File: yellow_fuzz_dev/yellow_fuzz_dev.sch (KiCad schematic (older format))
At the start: 39 parts

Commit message: pulling parts in for schematic capture
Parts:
- added C?: 47n, Capacitor_SMD:C_0603_1608Metric_Pad1.05x0.95mm_HandSolder, symbol Device:C
- added CON?: SN49B12B, digikey-footprints:Headphone_Jack_6.35mm_SN49B12B, symbol dk_Barrel-Audio-Connectors:SN49B12B
- added D?: WP7113QBC_D, digikey-footprints:LED_5mm_Radial, symbol dk_LEDs:WP7113QBC_D
- added J?: RA49B11, yellow_fuzz_dev:Headphone_Jack_6.35mm_SN49B12B, symbol yellow_fuzz_dev:RA49B11
- added Q?: NSVJ3910SB3T1GOSCT-ND, Package_TO_SOT_SMD:SOT-23_Handsoldering, symbol yellow_fuzz_dev:NSVJ3910SB3T1GOSCT-ND
- added Q?: BC817-25-TP, digikey-footprints:SOT-23-3, symbol dk_NPN_Single:BC817-25-TP
- added R? (x2): 10k, Resistor_SMD:R_0603_1608Metric_Pad1.05x0.95mm_HandSolder, symbol Device:R
- added R?: 1M, Resistor_SMD:R_0603_1608Metric_Pad1.05x0.95mm_HandSolder, symbol Device:R
- added U? (x5): TL074, digikey:SOIC-14_W3.9mm, symbol Amplifier_Operational:TL074
- RV?: footprint Potentiometer_THT:Potentiometer_Alps_RK09L_Single_Vertical -> yellow_fuzz_dev:Potentiometer_Bourns_PCW1J_R24_B_Single_Vertical; Manufacturer ALPS -> Bourns; Manufacturer PN RK09L1140A5P -> PTV111-4420A-A503; Supplier PN 688-RK09L1140A5P -> 652-PTV111-4420AA503; Taper Linear -> Log
- RV?: footprint Potentiometer_THT:Potentiometer_Alps_RK09Y11_Single_Horizontal -> yellow_fuzz_dev:Potentiometer_Bourns_PCW1J_R24_B_Single_Vertical; Manufacturer ALPS -> Bourns; Manufacturer PN RK09L1140A65 -> PCW1J-R24-BAD252; Supplier PN 688-RK09L1140A65 -> 652-PCW1J-R24-BAD252; Taper Linear -> Log; Value 5k -> 2.5k
- RV?: footprint Potentiometer_THT:Potentiometer_Alps_RK09L_Double_Vertical -> yellow_fuzz_dev:Potentiometer_Bourns_PTV112_3417A_Dual_Vertical; Manufacturer ALPS -> Bourns; Manufacturer PN RK09L124000Z -> PTV112-4420A-A503; Supplier PN 688-RK09L124000Z -> 652-PTV112-4420AA503; Taper Linear -> Log
- RV?: footprint Potentiometer_THT:Potentiometer_Alps_RK09L_Double_Vertical -> yellow_fuzz_dev:Potentiometer_Bourns_PTV112_3417A_Dual_Vertical; Manufactuerer PN RK09L124000Z -> PTV112-4420A-A503; Manufacturer ALPS -> Bourns; Supplier PN 688-RK09L124000Z -> 652-PTV112-4420AA503; Taper Linear -> Log
- RV?: footprint Potentiometer_THT:Potentiometer_Alps_RK09L_Single_Vertical -> Potentiometer_THT:Potentiometer_Bourns_PTV09A-1_Single_Vertical; Manufacturer ALPS -> Bourns; Manufacturer PN RK09D113BF25B15 -> PTV09A-4030U-A204; Supplier PN 688-RK09D113BF25B15 -> 652-PTV09A-4030UA204; Taper Linear -> Log; Value 100k -> 200k
- RV?: footprint Potentiometer_THT:Potentiometer_TT_P0915N -> yellow_fuzz_dev:Potentiometer_Bourns_PTV111_4420A_Single_Vertical; Manufacturer (none) -> Bourns; Manufacturer PN (none) -> PTV111-4420A-A104; Supplier (none) -> Mouser; Supplier PN (none) -> 652-PTV111-4420AA104; Value 250k -> 100k
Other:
- moved on the sheet: C?, R?, RV?, RV?A, RV?B

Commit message: schematic capture in progress
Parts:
- removed U?: TL074, digikey:SOIC-14_W3.9mm, symbol Amplifier_Operational:TL074
- added C? (x3): 1u, symbol Device:CP1
- added C? (x3): 15n, Capacitor_SMD:C_0603_1608Metric_Pad1.05x0.95mm_HandSolder, symbol Device:C
- added C? (x2): 47n, Capacitor_SMD:C_0603_1608Metric_Pad1.05x0.95mm_HandSolder, symbol Device:C
- added C?: 33n, Capacitor_SMD:C_0603_1608Metric_Pad1.05x0.95mm_HandSolder, symbol Device:C
- added C?: 220p, Capacitor_SMD:C_0603_1608Metric_Pad1.05x0.95mm_HandSolder, symbol Device:C
- added C?: 27n, Capacitor_SMD:C_0603_1608Metric_Pad1.05x0.95mm_HandSolder, symbol Device:C
- added C?: 10n, Capacitor_SMD:C_0603_1608Metric_Pad1.05x0.95mm_HandSolder, symbol Device:C
- added C? (x2): 47p, Capacitor_SMD:C_0603_1608Metric_Pad1.05x0.95mm_HandSolder, symbol Device:C
- added C? (x4): 10u, symbol Device:CP1
- added C?: 10p, Capacitor_SMD:C_0603_1608Metric_Pad1.05x0.95mm_HandSolder, symbol Device:C
- added C?: 220n, symbol Device:CP1
- added C?: 1.5n, Capacitor_SMD:C_0603_1608Metric_Pad1.05x0.95mm_HandSolder, symbol Device:C
- added D? (x2): 1N4148, digikey-footprints:Diode_DO-35_P10mm, symbol dk_Diodes-Rectifiers-Single:1N4148
- added Q? (x2): NSVJ3910SB3T1GOSCT-ND, Package_TO_SOT_SMD:SOT-23_Handsoldering, symbol yellow_fuzz_dev:NSVJ3910SB3T1GOSCT-ND
- added Q? (x4): BC817-25-TP, digikey-footprints:SOT-23-3, symbol dk_NPN_Single:BC817-25-TP
- added R? (x6): 100k, Resistor_SMD:R_0603_1608Metric_Pad1.05x0.95mm_HandSolder, symbol Device:R
- added R? (x2): 1M, Resistor_SMD:R_0603_1608Metric_Pad1.05x0.95mm_HandSolder, symbol Device:R
- added R? (x9): 10k, Resistor_SMD:R_0603_1608Metric_Pad1.05x0.95mm_HandSolder, symbol Device:R
- added R?: 220k, Resistor_SMD:R_0603_1608Metric_Pad1.05x0.95mm_HandSolder, symbol Device:R
- added R? (x2): 47k, Resistor_SMD:R_0603_1608Metric_Pad1.05x0.95mm_HandSolder, symbol Device:R
- added R? (x2): 2.2k, Resistor_SMD:R_0603_1608Metric_Pad1.05x0.95mm_HandSolder, symbol Device:R
- added R? (x3): 1k, Resistor_SMD:R_0603_1608Metric_Pad1.05x0.95mm_HandSolder, symbol Device:R
- added R?: 4.7k, Resistor_SMD:R_0603_1608Metric_Pad1.05x0.95mm_HandSolder, symbol Device:R
- added R? (x3): 22k, Resistor_SMD:R_0603_1608Metric_Pad1.05x0.95mm_HandSolder, symbol Device:R
- added R?: 3.3k, Resistor_SMD:R_0603_1608Metric_Pad1.05x0.95mm_HandSolder, symbol Device:R
- added R?: 470k, Resistor_SMD:R_0603_1608Metric_Pad1.05x0.95mm_HandSolder, symbol Device:R
- added U?: TL074, symbol Amplifier_Operational:TL074
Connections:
- net labels added: +4V5, +9V, GND
- wire segments 0 -> 186
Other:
- note added: "Here Lies Clippy"
- note added: "Input Buffer"
- note added: "Post Distortion"
- note added: "Pre-Distortion"
- moved on the sheet: C?, J?, Q?, R?, RV?, RV?A, RV?B, U?B, U?C, U?D, U?E

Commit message: placing symbols for EQ section
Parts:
- removed RV?: R_POT_Dual_Separate, yellow_fuzz_dev:Potentiometer_Bourns_PTV112_3417A_Dual_Vertical, symbol Device:R_POT_Dual_Separate
- added C?: 10p, Capacitor_SMD:C_0603_1608Metric_Pad1.05x0.95mm_HandSolder, symbol Device:C
- added C? (x2): 1u, symbol Device:CP1
- added C?: 100p, Capacitor_SMD:C_0603_1608Metric_Pad1.05x0.95mm_HandSolder, symbol Device:C
- added C?: 10n, Capacitor_SMD:C_0603_1608Metric_Pad1.05x0.95mm_HandSolder, symbol Device:C
- added C?: 220n, symbol Device:CP1
- added C?: 47n, Capacitor_SMD:C_0603_1608Metric_Pad1.05x0.95mm_HandSolder, symbol Device:C
- added C?: 0.1u, Capacitor_SMD:C_0603_1608Metric_Pad1.05x0.95mm_HandSolder, symbol Device:C
- added C?: 8.2n, Capacitor_SMD:C_0603_1608Metric_Pad1.05x0.95mm_HandSolder, symbol Device:C
- added C?: 22n, Capacitor_SMD:C_0603_1608Metric_Pad1.05x0.95mm_HandSolder, symbol Device:C
- added C?: 10u, symbol Device:CP1
- added R?: 22k, Resistor_SMD:R_0603_1608Metric_Pad1.05x0.95mm_HandSolder, symbol Device:R
- added R? (x2): 47k, Resistor_SMD:R_0603_1608Metric_Pad1.05x0.95mm_HandSolder, symbol Device:R
- added R? (x2): 330, Resistor_SMD:R_0603_1608Metric_Pad1.05x0.95mm_HandSolder, symbol Device:R
- added R? (x3): 2.2k, Resistor_SMD:R_0603_1608Metric_Pad1.05x0.95mm_HandSolder, symbol Device:R
- added R?: 100k, Resistor_SMD:R_0603_1608Metric_Pad1.05x0.95mm_HandSolder, symbol Device:R
- added R?: 1M, Resistor_SMD:R_0603_1608Metric_Pad1.05x0.95mm_HandSolder, symbol Device:R
- added RV? (x3): R_POT_US, yellow_fuzz_dev:Potentiometer_Bourns_PTV111_4420A_Single_Vertical, symbol Device:R_POT_US
- added RV?: R_POT_Dual_Separate, yellow_fuzz_dev:Potentiometer_Bourns_PTV112_3417A_Dual_Vertical, symbol Device:R_POT_Dual_Separate
- added U?: TL074, symbol Amplifier_Operational:TL074
- added U? (x4): TL074, digikey:SOIC-14_W3.9mm, symbol Amplifier_Operational:TL074
- CON?: symbol dk_Barrel-Audio-Connectors:SN49B12B -> yellow_fuzz_dev-rescue:SN49B12B-dk_Barrel-Audio-Connectors
- D? (x2): symbol dk_Diodes-Rectifiers-Single:1N4148 -> yellow_fuzz_dev-rescue:1N4148-dk_Diodes-Rectifiers-Single
- D?: symbol dk_LEDs:WP7113QBC_D -> yellow_fuzz_dev-rescue:WP7113QBC_D-dk_LEDs
- Q? (x5): symbol dk_NPN_Single:BC817-25-TP -> yellow_fuzz_dev-rescue:BC817-25-TP-dk_NPN_Single
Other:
- note removed: "Here Lies Clippy"
- note removed: "Input Buffer"
- note removed: "Post Distortion"
- note removed: "Pre-Distortion"
- moved on the sheet: RV?, RV?B

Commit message: captured tone, power, and switching sections.
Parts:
- added C?: 1u, symbol Device:CP1
- added C? (x3): 100u, symbol Device:CP1
- added C?: 47n, Capacitor_SMD:C_0603_1608Metric_Pad1.05x0.95mm_HandSolder, symbol Device:C
- added C?: 10n, Capacitor_SMD:C_0603_1608Metric_Pad1.05x0.95mm_HandSolder, symbol Device:C
- added C? (x2): 220p, Capacitor_SMD:C_0603_1608Metric_Pad1.05x0.95mm_HandSolder, symbol Device:C
- added C? (x2): 470p, Capacitor_SMD:C_0603_1608Metric_Pad1.05x0.95mm_HandSolder, symbol Device:C
- added D? (x3): BAS16W, Package_TO_SOT_SMD:SOT-323_SC-70, symbol Diode:BAS16W
- added D?: DZ2S056X0L, Diode_SMD:D_SOD-523, symbol Diode:DZ2S056X0L
- added J?: Barrel_Jack_Switch, symbol Connector:Barrel_Jack_Switch
- added Q?: NSVJ3910SB3T1GOSCT-ND, Package_TO_SOT_SMD:SOT-23_Handsoldering, symbol yellow_fuzz_dev:NSVJ3910SB3T1GOSCT-ND
- added Q? (x2): BC817-25-TP, digikey-footprints:SOT-23-3, symbol yellow_fuzz_dev-rescue:BC817-25-TP-dk_NPN_Single
- added Q? (x2): DMG2301L, Package_TO_SOT_SMD:SOT-23, symbol Transistor_FET:DMG2301L
- added R?: 2.2k, Resistor_SMD:R_0603_1608Metric_Pad1.05x0.95mm_HandSolder, symbol Device:R
- added R? (x4): 1M, Resistor_SMD:R_0603_1608Metric_Pad1.05x0.95mm_HandSolder, symbol Device:R
- added R?: 1.2k, Resistor_SMD:R_0603_1608Metric_Pad1.05x0.95mm_HandSolder, symbol Device:R
- added R? (x2): 10k, Resistor_SMD:R_0603_1608Metric_Pad1.05x0.95mm_HandSolder, symbol Device:R
- added R?: 100, Resistor_SMD:R_0603_1608Metric_Pad1.05x0.95mm_HandSolder, symbol Device:R
- added R? (x2): 100k, Resistor_SMD:R_0603_1608Metric_Pad1.05x0.95mm_HandSolder, symbol Device:R
- added R? (x4): 56k, Resistor_SMD:R_0603_1608Metric_Pad1.05x0.95mm_HandSolder, symbol Device:R
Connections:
- net +4V: now also R?.2, R?.2, C?.1, C?.1, R?.1, R?.1, R?.1, R?.2
- net +9V: now also C?.1, D?.1 (K), R?.1, R?.1, R?.1, R?.1
- net GND: now also C?.2, C?.2, R?.2, RV?.1, C?.2, C?.2, C?.2, C?.2, C?.2, Q?.2 (E), Q?.2 (E), R?.2, R?.2, R?.2
- net at RV?.2: now also C?.2
- net at RV?.3: now also C?.2
- net at RV?.4: now also C?.1, C?.1, RV?.1, RV?.2, RV?.5
- net at RV?.6: now also R?.1
- net at Q?.3 (G): now also D?.1 (A) (x2)
- net at D?.1: now also R?.2
- net at U?.1: now also R?.2, U?.2 (-)
- net at U?.3 (+): now also C?.2, R?.1
- net at U?.5 (+): now also RV?.1, RV?.1
- net at U?.6 (-): now also C?.2, R?.2, RV?.3, RV?.3
- net at U?.7: now also C?.1, C?.2, R?.1
- net at U?.10 (+): now also C?.2, R?.1
- net at U?.8: now also C?.1, C?.1, C?.2, R?.1
- net at U?.9 (-): now also C?.2, R?.1, R?.2
- net at U?.12 (+): now also RV?.2
- net at U?.13 (-): now also C?.1, U?.14
- net at C?.1: now also R?.1, R?.2
- net at C?.1: now also R?.1
- net at R?.2: now also RV?.1
- net at R?.1: now also RV?.2
- net at R?.2: now also C?.1
- net at R?.1: now also C?.1, C?.2
- net at C?.1: now also RV?.2
- net at R?.2: now also RV?.3
- net at RV?.3: now also R?.2
- net at C?.2: now also R?.1
- new net: C?.1, Q?.1 (S), R?.2
- new net: Q?.2 (D), R?.2
- new net: D?.1 (A), Q?.3 (G)
- new net: D?.2 (A), R?.1
- new net: C?.1, C?.2, Q?.1 (B), R?.1, R?.2
- new net: C?.2, Q?.3 (C), R?.1, R?.2, R?.2
- new net: C?.1, C?.1, Q?.1 (B), R?.1, R?.1
- new net: C?.1, Q?.3 (C), R?.1, R?.2
- new net: C?.1, C?.2, C?.2, R?.1, R?.2
- new net: C?.1, R?.2
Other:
- note added: "Active\n"
- note added: "Dist"
- note added: "High"
- note added: "Level\n"
- note added: "Low"
- note added: "Mid Freq\n"
- note added: "Mid\n"
- moved on the sheet: C?, D?, J?, Q?, R?, RV?, RV?A, RV?B, U?A, U?B, U?C, U?D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

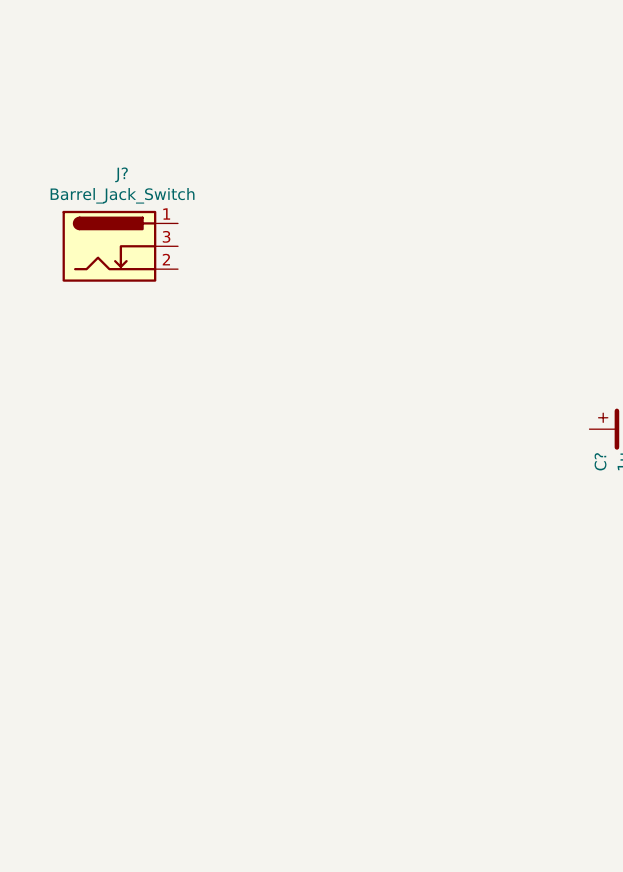
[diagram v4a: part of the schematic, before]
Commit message: added power jack
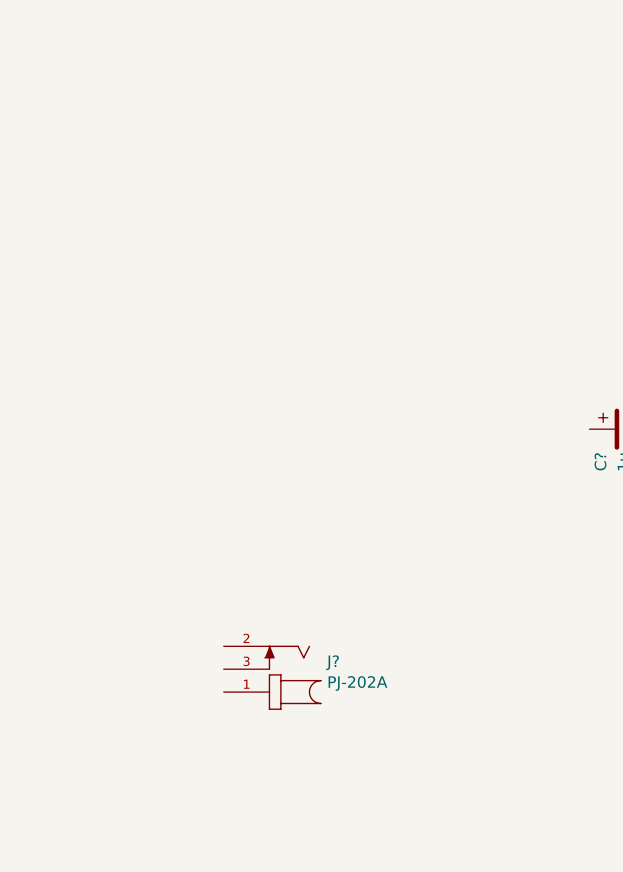
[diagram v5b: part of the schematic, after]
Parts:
- removed J?: Barrel_Jack_Switch, symbol Connector:Barrel_Jack_Switch
- added J?: PJ-202A, CUI_PJ-202A, symbol PJ-202A:PJ-202A
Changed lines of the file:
@@
-$EndComp
-$Comp
-L Connector:Barrel_Jack_Switch J?
-U 1 1 5F1031A8
-P 1400 6600
-F 0 "J?" H 1457 6917 50  0000 C CNN
-F 1 "Barrel_Jack_Switch" H 1457 6826 50  0000 C CNN
-F 2 "" H 1450 6560 50  0001 C CNN
-F 3 "~" H 1450 6560 50  0001 C CNN
-	1    1400 6600
-	1    0    0    -1
 $EndComp
 $Comp
@@
 Wire Wire Line
 	2950 14550 2950 14650
+$Comp
+L PJ-202A:PJ-202A J?
+U 1 1 5E83659F
+P 2100 8450
+F 0 "J?" H 1848 8417 50  0000 R CNN
+F 1 "PJ-202A" H 1848 8508 50  0000 R CNN
+F 2 "CUI_PJ-202A" H 2100 8450 50  0001 L BNN
+F 3 "Manufacturer recommendations" H 2100 8450 50  0001 L BNN
+F 4 "1.02" H 2100 8450 50  0001 L BNN "Field4"
+F 5 "CUI INC" H 2100 8450 50  0001 L BNN "Field5"
+F 6 "CUI" H 2100 8450 50  0001 C CNN "Manufacturer"
+F 7 "PJ-202A" H 2100 8450 50  0001 C CNN "Manufacturer Part Number"
+F 8 "Digi-Key" H 2100 8450 50  0001 C CNN "Supplier"
+F 9 "CP-202A-ND" H 2100 8450 50  0001 C CNN "Supplier Part Number"
+	1    2100 8450
+	-1   0    0    1
+$EndComp
 $EndSCHEMATC

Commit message: power section and interconnect done
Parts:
- removed Q? (x2): DMG2301L, Package_TO_SOT_SMD:SOT-23, symbol Transistor_FET:DMG2301L
- added BAT?: BC9VPC, digikey-footprints:Battery_Holder_9V_BC9VPC-ND, symbol dk_Battery-Holders-Clips-Contacts:BC9VPC
- added C? (x2): 0.1u, Capacitor_SMD:C_0603_1608Metric_Pad1.05x0.95mm_HandSolder, symbol Device:C
- added Q? (x2): DMN2041L, Package_TO_SOT_SMD:SOT-23, symbol Transistor_FET:DMN2041L
- added R?: 10k, Resistor_SMD:R_0603_1608Metric_Pad1.05x0.95mm_HandSolder, symbol Device:R
- added S?: 1825910-6, digikey-footprints:Switch_Tactile_THT_6x6mm, symbol dk_Tactile-Switches:1825910-6
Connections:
- net +9V: now also U?.4 (V+), U?.4 (V+), C?.1, C?.1, R?.2
- net GND: now also U?.11 (V-), U?.11 (V-), C?.2, C?.2, Q?.2 (S), S?.1, S?.2
- net INPUT_RING: now reaches CON?.R
- net INPUT_RING: now also Q?.2 (S)
- net at C?.1: now also Q?.2 (D), R?.1, R?.2
- net BYPASS_EN: now reaches D?.2
- net BYPASS_EN: now also C?.1, D?.3 (K), Q?.3 (C), R?.1, R?.2
- net at RV?.1, RV?.1, U?.5 (+): now also R?.1
- net at C?.1, Q?.2 (D): now also Q?.2 (D), R?.2
- net at J?.1: now also Q?.3 (D)
- net at J?.2: now also Q?.1 (G), R?.1
- net at J?.3: now also BAT?.POS, Q?.1 (G)
- net DIST_IN_EN: now reaches D?.3 (K)
- net DIST_IN_EN: now also C?.2, D?.3 (K), Q?.3 (C), R?.1, R?.2, R?.2
- net SW_BASE_A: now reaches C?.1, C?.2, Q?.1 (B), R?.1, R?.2
- net SW_BASE_B: now reaches C?.1, C?.1, Q?.1 (B), R?.1, R?.1
- net SW_IN_DB: now reaches C?.1, C?.2, C?.2, R?.1, R?.2
- net SW_IN: now reaches R?.2
- net SW_IN: now also S?.3, S?.4
- new net: BAT?.NEG, Q?.3 (D)
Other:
- note added: "Input"
- note added: "LED"
- note added: "Output"
- note added: "Power"
- note added: "Switching"
- note removed: "Active\n"
- moved on the sheet: C?, CON?, D?, J?, Q?, R?, RV?, U?A, U?B, U?C, U?D, U?E

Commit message: Changed qual op amps to duals for easy swapping
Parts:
- removed C?: 10p, Capacitor_SMD:C_0603_1608Metric_Pad1.05x0.95mm_HandSolder, symbol Device:C
- removed C?: 220n, symbol Device:CP1
- removed C?: 47p, Capacitor_SMD:C_0603_1608Metric_Pad1.05x0.95mm_HandSolder, symbol Device:C
- removed C?: 220p, Capacitor_SMD:C_0603_1608Metric_Pad1.05x0.95mm_HandSolder, symbol Device:C
- removed C?: 470p, Capacitor_SMD:C_0603_1608Metric_Pad1.05x0.95mm_HandSolder, symbol Device:C
- removed C?: 1.5n, Capacitor_SMD:C_0603_1608Metric_Pad1.05x0.95mm_HandSolder, symbol Device:C
- removed C?: 8.2n, Capacitor_SMD:C_0603_1608Metric_Pad1.05x0.95mm_HandSolder, symbol Device:C
- removed C?: 10n, Capacitor_SMD:C_0603_1608Metric_Pad1.05x0.95mm_HandSolder, symbol Device:C
- removed C?: 15n, Capacitor_SMD:C_0603_1608Metric_Pad1.05x0.95mm_HandSolder, symbol Device:C
- removed C?: 22n, Capacitor_SMD:C_0603_1608Metric_Pad1.05x0.95mm_HandSolder, symbol Device:C
- removed C?: 27n, Capacitor_SMD:C_0603_1608Metric_Pad1.05x0.95mm_HandSolder, symbol Device:C
- removed C?: 33n, Capacitor_SMD:C_0603_1608Metric_Pad1.05x0.95mm_HandSolder, symbol Device:C
- removed C?: 47n, Capacitor_SMD:C_0603_1608Metric_Pad1.05x0.95mm_HandSolder, symbol Device:C
- removed C? (x3): 0.1u, Capacitor_SMD:C_0603_1608Metric_Pad1.05x0.95mm_HandSolder, symbol Device:C
- removed C?: 1u, symbol Device:CP1
- removed C?: 10u, symbol Device:CP1
- removed C? (x2): 100u, symbol Device:CP1
- removed R?: 100, Resistor_SMD:R_0603_1608Metric_Pad1.05x0.95mm_HandSolder, symbol Device:R
- removed R?: 330, Resistor_SMD:R_0603_1608Metric_Pad1.05x0.95mm_HandSolder, symbol Device:R
- removed R?: 1k, Resistor_SMD:R_0603_1608Metric_Pad1.05x0.95mm_HandSolder, symbol Device:R
- removed R?: 1.2k, Resistor_SMD:R_0603_1608Metric_Pad1.05x0.95mm_HandSolder, symbol Device:R
- removed R?: 2.2k, Resistor_SMD:R_0603_1608Metric_Pad1.05x0.95mm_HandSolder, symbol Device:R
- removed R?: 3.3k, Resistor_SMD:R_0603_1608Metric_Pad1.05x0.95mm_HandSolder, symbol Device:R
- removed R?: 4.7k, Resistor_SMD:R_0603_1608Metric_Pad1.05x0.95mm_HandSolder, symbol Device:R
- removed R?: 10k, Resistor_SMD:R_0603_1608Metric_Pad1.05x0.95mm_HandSolder, symbol Device:R
- removed R?: 22k, Resistor_SMD:R_0603_1608Metric_Pad1.05x0.95mm_HandSolder, symbol Device:R
- removed R?: 47k, Resistor_SMD:R_0603_1608Metric_Pad1.05x0.95mm_HandSolder, symbol Device:R
- removed R?: 56k, Resistor_SMD:R_0603_1608Metric_Pad1.05x0.95mm_HandSolder, symbol Device:R
- removed R?: 100k, Resistor_SMD:R_0603_1608Metric_Pad1.05x0.95mm_HandSolder, symbol Device:R
- removed R?: 220k, Resistor_SMD:R_0603_1608Metric_Pad1.05x0.95mm_HandSolder, symbol Device:R
- removed R?: 470k, Resistor_SMD:R_0603_1608Metric_Pad1.05x0.95mm_HandSolder, symbol Device:R
- removed R?: 1M, Resistor_SMD:R_0603_1608Metric_Pad1.05x0.95mm_HandSolder, symbol Device:R
- removed RV?: R_POT_TRIM_US, yellow_fuzz_dev:Potentiometer_Bourns_PCW1J_R24_B_Single_Vertical, symbol Device:R_POT_TRIM_US
- removed RV?: R_POT_US, yellow_fuzz_dev:Potentiometer_Bourns_PTV111_4420A_Single_Vertical, symbol Device:R_POT_US
- removed U? (x8): TL074, digikey:SOIC-14_W3.9mm, symbol Amplifier_Operational:TL074
- removed U? (x2): TL074, symbol Amplifier_Operational:TL074
- added C?: 47n, Capacitor_SMD:C_0603_1608Metric_Pad1.05x0.95mm_HandSolder, symbol Device:C
- added C? (x4): 0.1u, Capacitor_SMD:C_0603_1608Metric_Pad1.05x0.95mm_HandSolder, symbol Device:C
- added R?: 470, Resistor_SMD:R_0603_1608Metric_Pad1.05x0.95mm_HandSolder, symbol Device:R
- added R?: 1M, Resistor_SMD:R_0603_1608Metric_Pad1.05x0.95mm_HandSolder, symbol Device:R
- added U? (x8): TL072CP, digikey-footprints:DIP-8_W7.62mm, symbol dk_opamps:TL072CP
- R?: value 10k -> 22; Manufacturer PN RC0603JR-071KL -> RC0603FR-0722RL; Supplier PN 311-1.0KGRCT-ND -> 311-22.0HRCT-ND
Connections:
- net +4V: now also R?.1, U?.5
- net +9V: now also C?.1, C?.1, C?.1, C?.1, U?.8 (VCC+), U?.8 (VCC+), U?.8 (VCC+), U?.8 (VCC+), U?.8 (VCC+), U?.8 (VCC+), U?.8 (VCC+), U?.8 (VCC+)
- net BYPASS_EN: now also R?.2; no longer D?.3 (K)
- net GND: now also C?.2, C?.2, C?.2, C?.2, C?.2, U?.4 (VCC-), U?.4 (VCC-), U?.4 (VCC-), U?.4 (VCC-), U?.4 (VCC-), U?.4 (VCC-), U?.4 (VCC-), U?.4 (VCC-)
- net LEVEL_OUT: now reaches C?.2, RV?.2
- net at C?.2, R?.1, RV?.1: now also U?.6
- net at C?.1, C?.1, RV?.2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: now also U?.7
- net BUFFERED_IN: now reaches C?.1, Q?.2 (D), R?.1, R?.2
- net at C?.1, R?.2: now also U?.3
- net at C?.1, R?.1, R?.2: now also U?.1 (x2)
- net at C?.1, R?.2: now also U?.5
- net at C?.1, C?.2, R?.2: now also U?.2
- net at C?.2, R?.2: now also U?.3
- net at C?.1, C?.1, C?.2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: now also U?.2
- net at C?.2, R?.2: now also R?.1, U?.6
- net at C?.1, R?.1, R?.2: now also U?.7
- net at R?.2: now also U?.6, U?.7
- net at C?.2, R?.1: now also U?.5
- net TONE_IN: now reaches R?.1, RV?.1, RV?.1
- net TONE_IN: now also U?.3
- net at C?.2, R?.2, RV?.3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: now also U?.2
- net at C?.1, C?.2, R?.1: now also U?.1
- net at C?.2, R?.1: now also U?.3
- net TONE_OUT: now reaches C?.1, C?.1, C?.2, R?.1
- net TONE_OUT: now also U?.1
- net at C?.2, R?.1, R?.2: now also U?.2
- net at RV?.2: now also U?.5
- net at C?.1: now also U?.6, U?.7
- net at Q?.2 (E), R?.1: now also R?.2
- net at C?.1, C?.2: now also R?.1
- new net: C?.1, D?.3 (K), R?.1
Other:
- note added: "Retuned pre-distortion boost filter."
- moved on the sheet: C?, R?
